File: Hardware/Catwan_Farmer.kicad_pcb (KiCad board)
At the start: 2 copper layers, 51.8 x 53.6 mm, 53 parts, among them J1 SENSOR 1, J10 VSP, J2 SENSOR 2, J3 SENSOR 3, J4 BATT, J5 USB_B, J6 SWD, J7 DHT22, J9 SENSOR 4, SW1 RST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

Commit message: New  netlist
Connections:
- D4 pad 1: Net-(D4-Pad1) -> /SENS_Y4
- D4 pad 2: Net-(D4-Pad2) -> /SENS_X4
- D5 pad 1: Net-(D5-Pad1) -> /SENS_Y2
- D5 pad 2: Net-(D5-Pad2) -> /SENS_X2
- D6 pad 1: Net-(D6-Pad1) -> /SENS_X3
- D6 pad 2: Net-(D6-Pad2) -> /SENS_Y3
- D8 pad 1: Net-(D8-Pad1) -> /SENS_Y1
- D8 pad 2: Net-(D8-Pad2) -> /SENS_X1
- J1 pad 1: Net-(D8-Pad1) -> /SENS_X1
- J1 pad 2: Net-(D8-Pad2) -> /SENS_Y1
- J2 pad 1: Net-(D5-Pad1) -> /SENS_X2
- J2 pad 2: Net-(D5-Pad2) -> /SENS_Y2
- J3 pad 1: Net-(D6-Pad2) -> /SENS_X3
- J3 pad 2: Net-(D6-Pad1) -> /SENS_Y3
- J9 pad 1: Net-(D4-Pad1) -> /SENS_X4
- J9 pad 2: Net-(D4-Pad2) -> /SENS_Y4
- U5 pad 1: Net-(D6-Pad2) -> /SENS_Y1
- U5 pad 11: Net-(D5-Pad2) -> /SENS_X4
- U5 pad 12: Net-(D8-Pad1) -> /SENS_X1
- U5 pad 14: Net-(D8-Pad2) -> /SENS_X2
- U5 pad 15: Net-(D5-Pad1) -> /SENS_X3
- U5 pad 2: Net-(D4-Pad1) -> /SENS_Y3
- U5 pad 4: Net-(D4-Pad2) -> /SENS_Y4
- U5 pad 5: Net-(D6-Pad1) -> /SENS_Y2
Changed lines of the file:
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@@
-(kicad_pcb (version 20171130) (host pcbnew "(5.1.5-0-10_14)")
+(kicad_pcb (version 20171130) (host pcbnew "(5.1.4-0-10_14)")
   (general
     (thickness 1.6)
@@
     (zones 0)
     (modules 53)
-    (nets 50)
+    (nets 58)
   )
   (page A4)
@@
   (net 48 "Net-(U2-Pad12)")
   (net 49 "Net-(U3-Pad8)")
+  (net 50 /SENS_Y4)
+  (net 51 /SENS_X4)
+  (net 52 /SENS_Y2)
+  (net 53 /SENS_X2)
+  (net 54 /SENS_Y3)
+  (net 55 /SENS_X3)
+  (net 56 /SENS_Y1)
+  (net 57 /SENS_X1)
   (net_class Default "This is the default net class."
     (clearance 0.2)
@@
     (add_net /SCK)
     (add_net /SENS_X)
+    (add_net /SENS_X1)
+    (add_net /SENS_X2)
+    (add_net /SENS_X3)
+    (add_net /SENS_X4)
     (add_net /SENS_Y)
+    (add_net /SENS_Y1)
+    (add_net /SENS_Y2)
+    (add_net /SENS_Y3)
+    (add_net /SENS_Y4)
     (add_net /SS)
     (add_net /SWCLK)
@@
     )
     (pad 2 thru_hole rect (at 0 0 180) (size 2.4 2.4) (drill 1.2) (layers *.Cu *.Mask)
-      (net 41 "Net-(D6-Pad1)"))
+      (net 54 /SENS_Y3))
     (pad 1 thru_hole circle (at 3.5 0 180) (size 2.4 2.4) (drill 1.2) (layers *.Cu *.Mask)
-      (net 40 "Net-(D6-Pad2)"))
+      (net 55 /SENS_X3))
     (model ${KISYS3DMOD}/TerminalBlock_Phoenix.3dshapes/TerminalBlock_Phoenix_PT-1,5-2-3.5-H_1x02_P3.50mm_Horizontal.wrl
       (at (xyz 0 0 0))
@@
     )
     (pad 1 smd roundrect (at -2.475 -4.445) (size 1.95 0.6) (layers F.Cu F.Paste F.Mask) (roundrect_rratio 0.25)
-      (net 40 "Net-(D6-Pad2)"))
+      (net 56 /SENS_Y1))
     (pad 2 smd roundrect (at -2.475 -3.175) (size 1.95 0.6) (layers F.Cu F.Paste F.Mask) (roundrect_rratio 0.25)
-      (net 36 "Net-(D4-Pad1)"))
+      (net 54 /SENS_Y3))
     (pad 3 smd roundrect (at -2.475 -1.905) (size 1.95 0.6) (layers F.Cu F.Paste F.Mask) (roundrect_rratio 0.25)
       (net 12 /SENS_Y))
     (pad 4 smd roundrect (at -2.475 -0.635) (size 1.95 0.6) (layers F.Cu F.Paste F.Mask) (roundrect_rratio 0.25)
-      (net 37 "Net-(D4-Pad2)"))
+      (net 50 /SENS_Y4))
     (pad 5 smd roundrect (at -2.475 0.635) (size 1.95 0.6) (layers F.Cu F.Paste F.Mask) (roundrect_rratio 0.25)
-      (net 41 "Net-(D6-Pad1)"))
+      (net 52 /SENS_Y2))
     (pad 6 smd roundrect (at -2.475 1.905) (size 1.95 0.6) (layers F.Cu F.Paste F.Mask) (roundrect_rratio 0.25)
       (net 19 /EN))
@@
       (net 17 /S0))
     (pad 11 smd roundrect (at 2.475 1.905) (size 1.95 0.6) (layers F.Cu F.Paste F.Mask) (roundrect_rratio 0.25)
-      (net 39 "Net-(D5-Pad2)"))
+      (net 51 /SENS_X4))
     (pad 12 smd roundrect (at 2.475 0.635) (size 1.95 0.6) (layers F.Cu F.Paste F.Mask) (roundrect_rratio 0.25)
-      (net 43 "Net-(D8-Pad1)"))
+      (net 57 /SENS_X1))
     (pad 13 smd roundrect (at 2.475 -0.635) (size 1.95 0.6) (layers F.Cu F.Paste F.Mask) (roundrect_rratio 0.25)
       (net 11 /SENS_X))
     (pad 14 smd roundrect (at 2.475 -1.905) (size 1.95 0.6) (layers F.Cu F.Paste F.Mask) (roundrect_rratio 0.25)
-      (net 42 "Net-(D8-Pad2)"))
+      (net 53 /SENS_X2))
     (pad 15 smd roundrect (at 2.475 -3.175) (size 1.95 0.6) (layers F.Cu F.Paste F.Mask) (roundrect_rratio 0.25)
-      (net 38 "Net-(D5-Pad1)"))
+      (net 55 /SENS_X3))
     (pad 16 smd roundrect (at 2.475 -4.445) (size 1.95 0.6) (layers F.Cu F.Paste F.Mask) (roundrect_rratio 0.25)
       (net 3 +3V3))
@@
     (fp_line (start 0.76 1.58) (end -0.7 1.58) (layer F.SilkS) (width 0.12))
     (pad 1 smd rect (at -1 -0.95 270) (size 0.9 0.8) (layers F.Cu F.Paste F.Mask)
-      (net 36 "Net-(D4-Pad1)"))
+      (net 50 /SENS_Y4))
     (pad 2 smd rect (at -1 0.95 270) (size 0.9 0.8) (layers F.Cu F.Paste F.Mask)
-      (net 37 "Net-(D4-Pad2)"))
+      (net 51 /SENS_X4))
     (pad 3 smd rect (at 1 0 270) (size 0.9 0.8) (layers F.Cu F.Paste F.Mask)
       (net 2 GND))
@@
     (fp_line (start 0.76 1.58) (end -0.7 1.58) (layer F.SilkS) (width 0.12))
     (pad 1 smd rect (at -1 -0.95 270) (size 0.9 0.8) (layers F.Cu F.Paste F.Mask)
-      (net 38 "Net-(D5-Pad1)"))
+      (net 52 /SENS_Y2))
     (pad 2 smd rect (at -1 0.95 270) (size 0.9 0.8) (layers F.Cu F.Paste F.Mask)
-      (net 39 "Net-(D5-Pad2)"))
+      (net 53 /SENS_X2))
     (pad 3 smd rect (at 1 0 270) (size 0.9 0.8) (layers F.Cu F.Paste F.Mask)
       (net 2 GND))
@@
       (net 2 GND))
     (pad 2 smd rect (at -1 0.95 270) (size 0.9 0.8) (layers F.Cu F.Paste F.Mask)
-      (net 40 "Net-(D6-Pad2)"))
+      (net 54 /SENS_Y3))
     (pad 1 smd rect (at -1 -0.95 270) (size 0.9 0.8) (layers F.Cu F.Paste F.Mask)
-      (net 41 "Net-(D6-Pad1)"))
+      (net 55 /SENS_X3))
     (model ${KISYS3DMOD}/Package_TO_SOT_SMD.3dshapes/SOT-23.wrl
       (at (xyz 0 0 0))
@@
     (fp_line (start 0.76 1.58) (end -0.7 1.58) (layer F.SilkS) (width 0.12))
     (pad 1 smd rect (at -1 -0.95 270) (size 0.9 0.8) (layers F.Cu F.Paste F.Mask)
-      (net 43 "Net-(D8-Pad1)"))
+      (net 56 /SENS_Y1))
     (pad 2 smd rect (at -1 0.95 270) (size 0.9 0.8) (layers F.Cu F.Paste F.Mask)
-      (net 42 "Net-(D8-Pad2)"))
+      (net 57 /SENS_X1))
     (pad 3 smd rect (at 1 0 270) (size 0.9 0.8) (layers F.Cu F.Paste F.Mask)
       (net 2 GND))
@@
     )
     (pad 1 thru_hole rect (at 0 0 180) (size 2.4 2.4) (drill 1.2) (layers *.Cu *.Mask)
-      (net 43 "Net-(D8-Pad1)"))
+      (net 57 /SENS_X1))
     (pad 2 thru_hole circle (at 3.5 0 180) (size 2.4 2.4) (drill 1.2) (layers *.Cu *.Mask)
-      (net 42 "Net-(D8-Pad2)"))
+      (net 56 /SENS_Y1))
     (model ${KISYS3DMOD}/TerminalBlock_Phoenix.3dshapes/TerminalBlock_Phoenix_PT-1,5-2-3.5-H_1x02_P3.50mm_Horizontal.wrl
       (at (xyz 0 0 0))
@@
     (fp_arc (start 0 0) (end 0 1.68) (angle -32) (layer F.SilkS) (width 0.12))
     (pad 2 thru_hole circle (at 3.5 0 180) (size 2.4 2.4) (drill 1.2) (layers *.Cu *.Mask)
-      (net 39 "Net-(D5-Pad2)"))
+      (net 52 /SENS_Y2))
     (pad 1 thru_hole rect (at 0 0 180) (size 2.4 2.4) (drill 1.2) (layers *.Cu *.Mask)
-      (net 38 "Net-(D5-Pad1)"))
+      (net 53 /SENS_X2))
     (model ${KISYS3DMOD}/TerminalBlock_Phoenix.3dshapes/TerminalBlock_Phoenix_PT-1,5-2-3.5-H_1x02_P3.50mm_Horizontal.wrl
       (at (xyz 0 0 0))
@@
     )
     (pad 1 thru_hole rect (at 0 0 180) (size 2.4 2.4) (drill 1.2) (layers *.Cu *.Mask)
-      (net 36 "Net-(D4-Pad1)"))
+      (net 51 /SENS_X4))
     (pad 2 thru_hole circle (at 3.5 0 180) (size 2.4 2.4) (drill 1.2) (layers *.Cu *.Mask)
-      (net 37 "Net-(D4-Pad2)"))
+      (net 50 /SENS_Y4))
     (model ${KISYS3DMOD}/TerminalBlock_Phoenix.3dshapes/TerminalBlock_Phoenix_PT-1,5-2-3.5-H_1x02_P3.50mm_Horizontal.wrl
       (at (xyz 0 0 0))
@@
     (connect_pads (clearance 0.508))
     (min_thickness 0.254)
-    (fill yes (arc_segments 32) (thermal_gap 0.508) (thermal_bridge_width 0.508))
+    (fill (arc_segments 32) (thermal_gap 0.508) (thermal_bridge_width 0.508))
     (polygon
       (pts
@@
     (connect_pads (clearance 0.508))
     (min_thickness 0.254)
-    (fill yes (arc_segments 32) (thermal_gap 0.508) (thermal_bridge_width 0.508))
+    (fill (arc_segments 32) (thermal_gap 0.508) (thermal_bridge_width 0.508))
     (polygon
       (pts

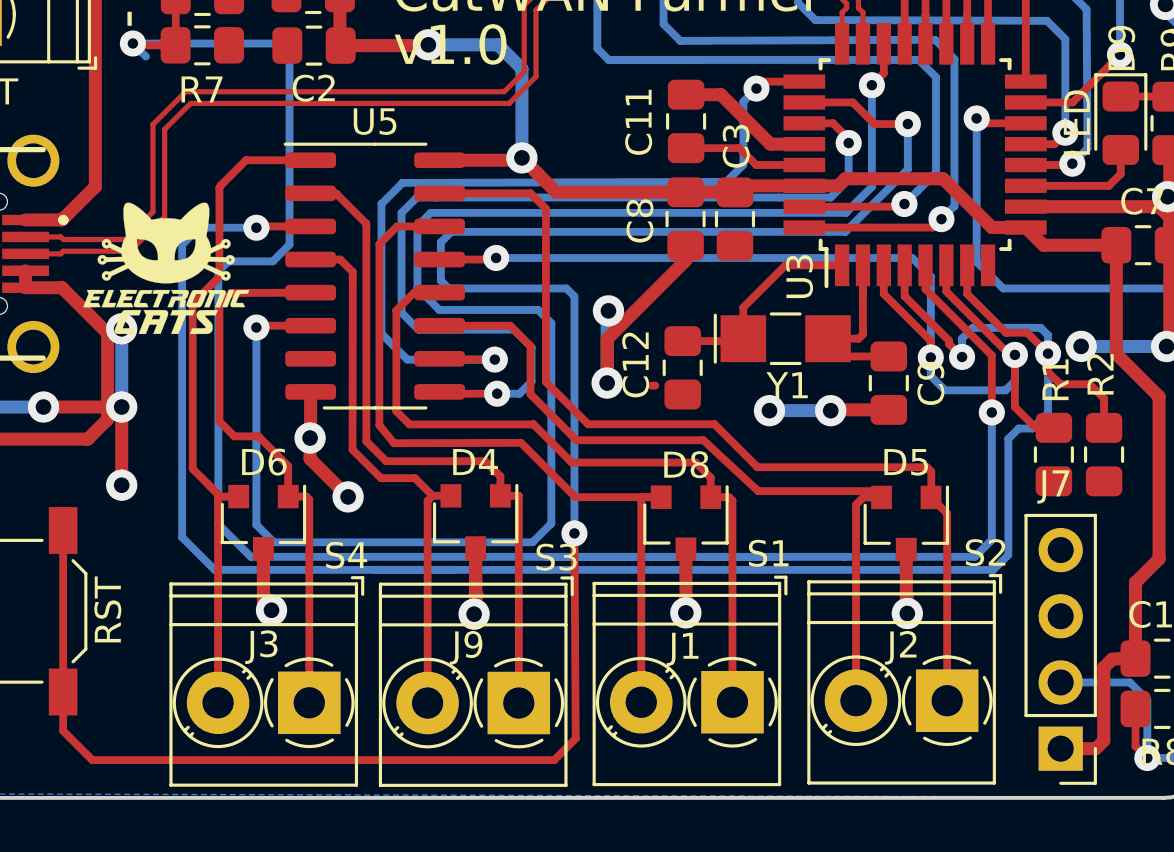
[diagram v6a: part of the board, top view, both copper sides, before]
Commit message: Change conn sensors
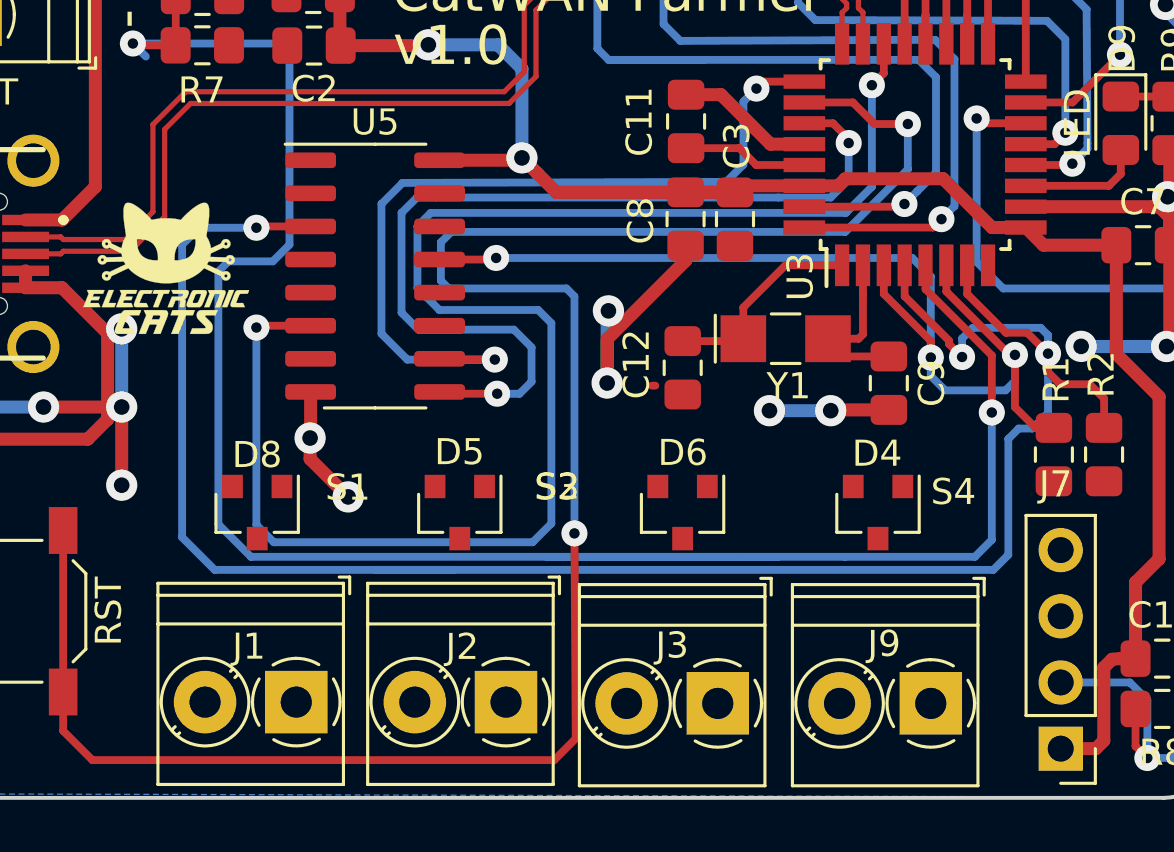
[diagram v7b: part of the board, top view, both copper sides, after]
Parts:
- moved svg2mod 18.7 mm to (153.9, 66.4)
- moved D5 17.1 mm to (138.0, 97.0)
- moved J2 16.9 mm to (139.8, 104.3)
- moved J1 16.7 mm to (131.7, 104.3)
- moved D8 16.5 mm to (130.2, 97.0)
- moved D6 16.1 mm to (146.5, 97.0)
- moved J9 15.8 mm to (156.1, 104.4)
- moved J3 15.7 mm to (147.9, 104.4)
- moved D4 15.4 mm to (154.0, 97.0)
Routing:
- net Net-(D5-Pad1): track 36.0 -> 0.00 mm
- net Net-(D8-Pad2): track 30.1 -> 0.00 mm
- net Net-(D5-Pad2): track 29.3 -> 0.00 mm
- net Net-(D8-Pad1): track 28.3 -> 0.00 mm
- net Net-(D4-Pad1): track 26.1 -> 0.00 mm
- net Net-(D6-Pad2): track 26.0 -> 0.00 mm
- net Net-(D6-Pad1): track 21.3 -> 0.00 mm
- net Net-(D4-Pad2): track 21.2 -> 0.00 mm
- net GND: track 134.6 -> 121.0 mm, vias 29 -> 25

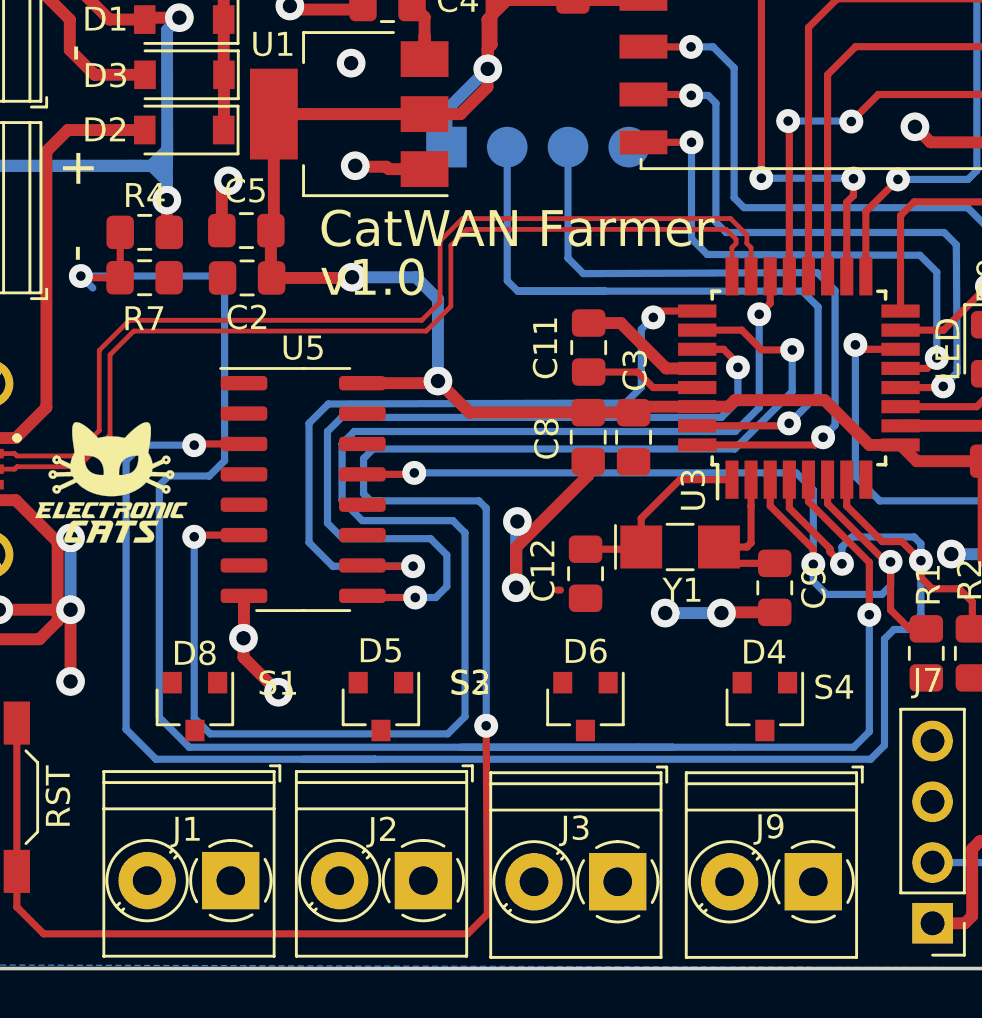
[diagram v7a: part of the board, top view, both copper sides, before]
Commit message: Change DI0 and CLK
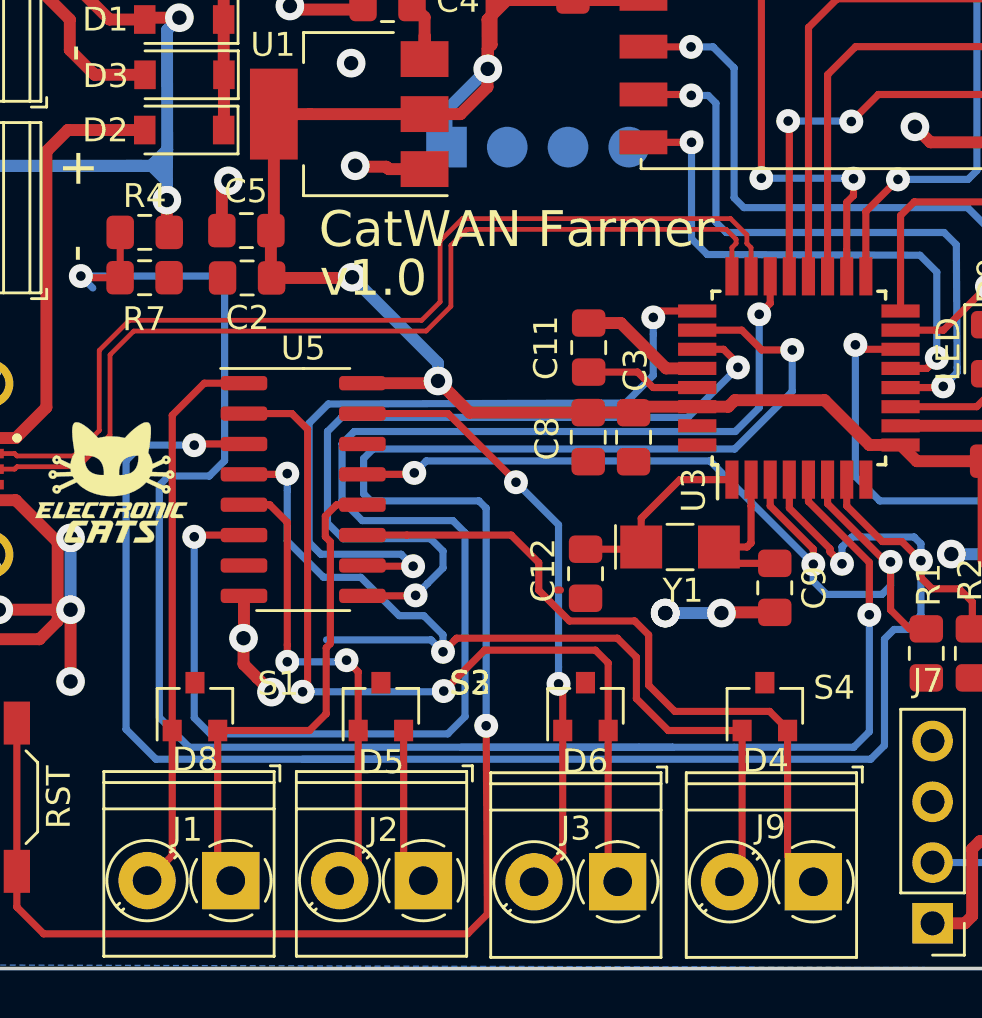
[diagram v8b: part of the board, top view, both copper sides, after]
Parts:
- turned D4 to 90 degrees
- turned D5 to 90 degrees
- turned D6 to 90 degrees
- turned D8 to 90 degrees
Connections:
- J6 pad 2: /SWCLK -> /SWDIO
- J6 pad 3: /SWDIO -> /SWCLK
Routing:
- net /SENS_Y4: track 0.00 -> 40.5 mm, vias 0 -> 2
- net /SENS_Y3: track 0.00 -> 37.0 mm, vias 0 -> 2
- net /SWCLK: track 32.2 -> 0.00 mm, vias 1 -> 0
- net /SENS_X4: track 0.00 -> 29.9 mm
- net /SWDIO: track 28.1 -> 0.00 mm, vias 1 -> 0
- net /SENS_X3: track 0.00 -> 25.6 mm, vias 0 -> 2
- net /SENS_Y1: track 0.00 -> 23.4 mm
- net /SENS_X1: track 0.00 -> 21.5 mm
- net /SENS_Y2: track 0.00 -> 20.2 mm, vias 0 -> 2
- net GND: track 121.0 -> 111.5 mm, vias 25 -> 24
- net /SENS_X2: track 0.00 -> 6.62 mm
- net +3V3: track 112.7 -> 111.1 mm
- net /S1: track 35.6 -> 34.1 mm
- net /SENS_X: track 40.4 -> 39.0 mm
